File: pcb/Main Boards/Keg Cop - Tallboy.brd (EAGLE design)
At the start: 65 x 51 mm, 17 parts, among them X1 RJ45-8X, X2 RJ45-8X

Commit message: Rename files
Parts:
- added ROOM: 3-PIN, Donnie:HDR-3_VERT
- moved U$1 2.80 mm to (4.50, 33.0)
- moved RELAY 0.49 mm to (13.4, 47.5)
- moved POWER 0.41 mm to (9.61, 41.9)
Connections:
- net 5V: now also ROOM.2
- net GND: now also ROOM.1
- net RDAT: now also ROOM.3
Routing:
- net RDAT: track 38.9 -> 43.6 mm
- net GND: track 255.8 -> 251.3 mm
- net SOL: track 78.7 -> 80.9 mm
- net TDAT: track 31.8 -> 30.9 mm
- net 3V3: track 40.1 -> 39.6 mm
- net LDAT: track 26.6 -> 26.1 mm
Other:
- board text added: "D"

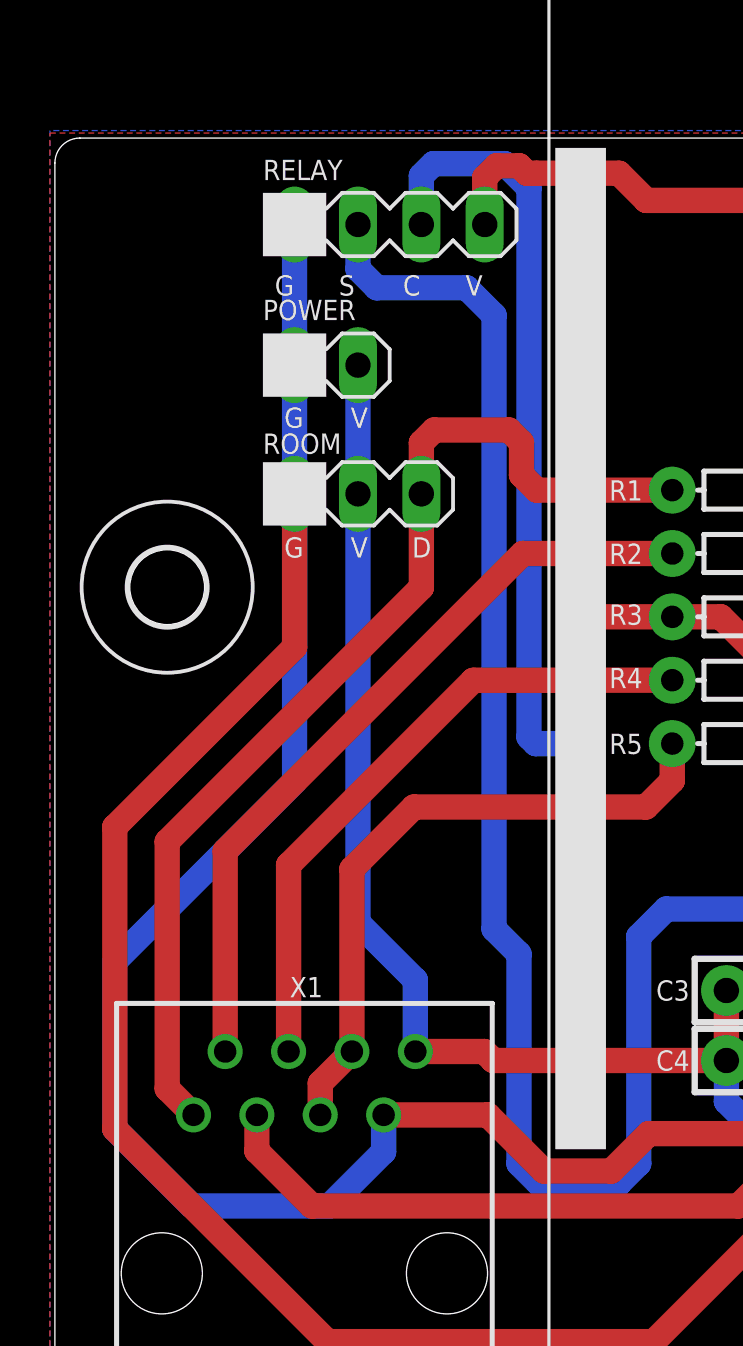
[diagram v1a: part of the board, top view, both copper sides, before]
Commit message: Add DS18B20 sensor
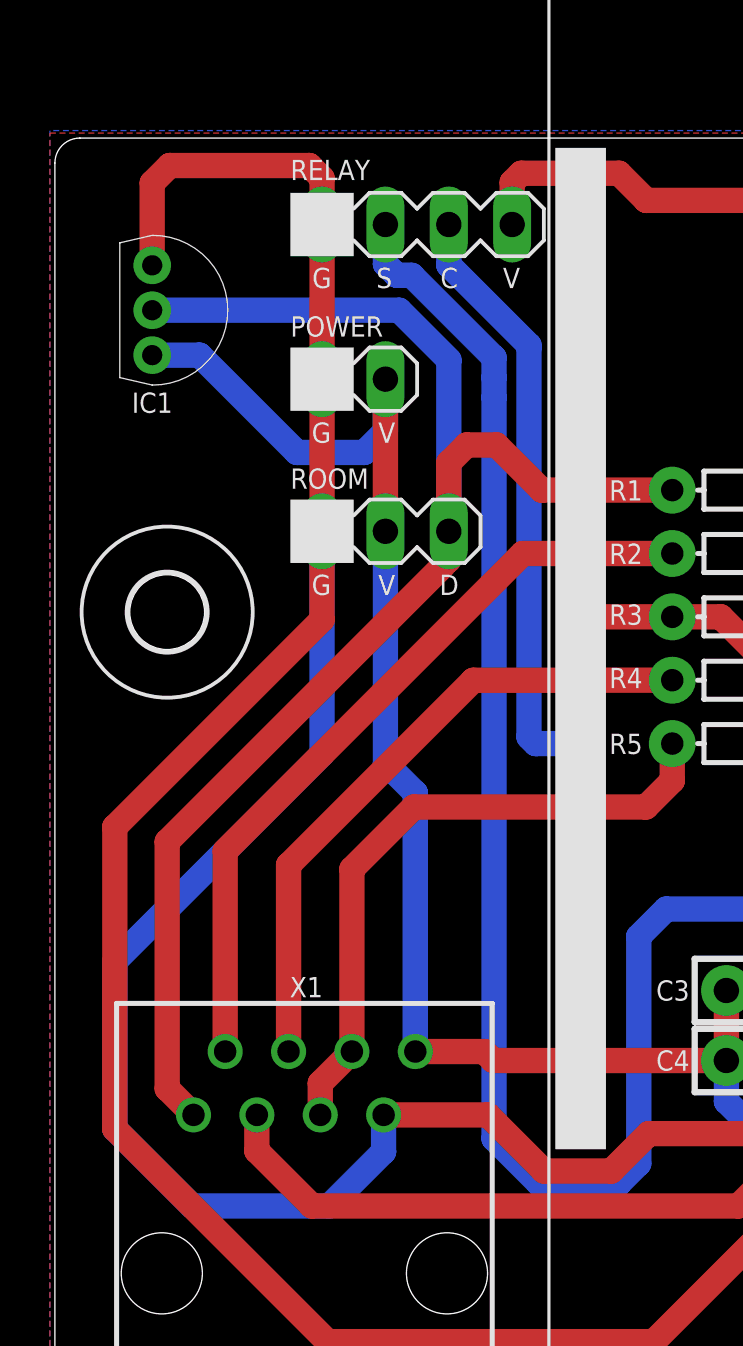
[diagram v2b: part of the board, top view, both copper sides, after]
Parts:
- added IC1: DS18B20+, SamacSys_Parts:TO-92
- moved ROOM 1.86 mm to (10.7, 35.2)
- moved POWER 1.24 mm to (10.7, 41.3)
- moved RELAY 1.10 mm to (14.5, 47.5)
- moved U$1 1.00 mm to (4.50, 32.0)
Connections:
- net 5V: now also IC1.3
- net GND: now also IC1.1
- net RDAT: now also IC1.2
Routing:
- net RDAT: track 43.6 -> 60.8 mm
- net 5V: track 81.5 -> 93.9 mm
- net GND: track 251.3 -> 263.2 mm
- net COOL: track 31.1 -> 24.0 mm
- net SOL: track 80.9 -> 78.7 mm
- net 3V3: track 39.6 -> 38.1 mm
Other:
- board text added: "1 - KEG1 2 - KEG2 3 - KEG3 4 - KEG4"
- board text added: "1 - RDAT 2 - TDAT 3 - UDAT 4 - LDAT"
- board text removed: "X1 1 - RDAT 2 - TDAT 3 - UDAT 4 - LDAT"
- board text removed: "X2 1 - KEG1 2 - KEG2 3 - KEG3 4 - KEG4"
